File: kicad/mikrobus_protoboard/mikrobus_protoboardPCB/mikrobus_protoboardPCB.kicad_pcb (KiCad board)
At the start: 2 copper layers, 26.8 x 57.5 mm, 0 parts

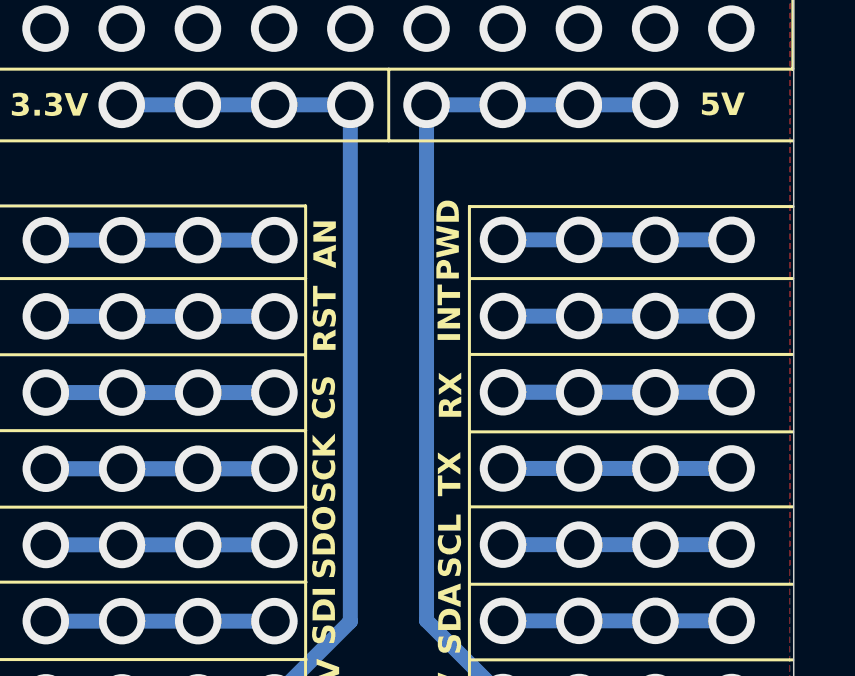
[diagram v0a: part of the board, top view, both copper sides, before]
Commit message: invert RX TX
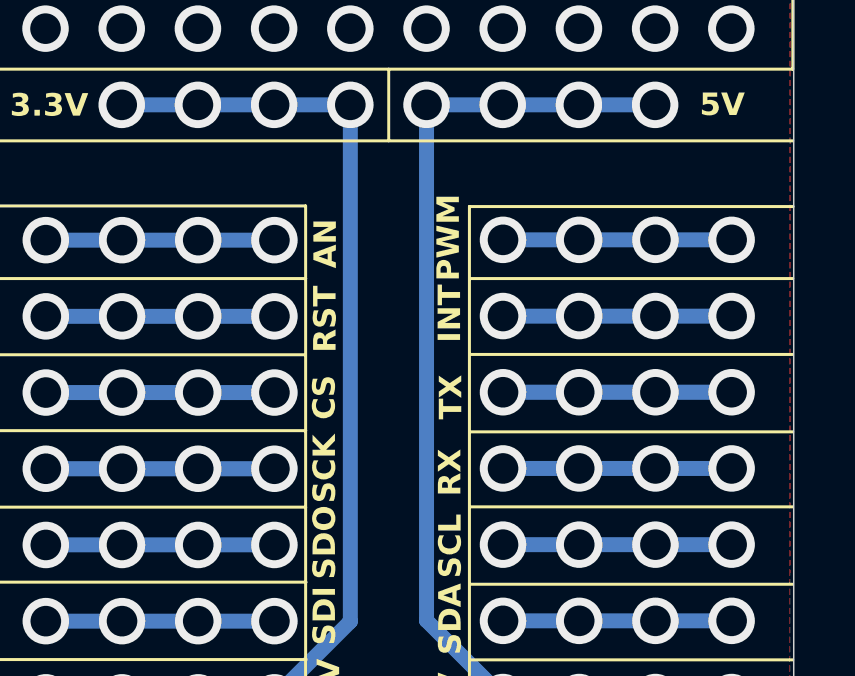
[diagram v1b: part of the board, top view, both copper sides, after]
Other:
- board text added: "PWM"
- board text removed: "PWD"
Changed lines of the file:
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@@
 	)
 	(paper "A4")
+	(title_block
+		(title "Mikrobus Protoboard")
+		(date "2024-09-03")
+		(rev "v1.1")
+		(company "Université Grenoble Alpes - CSUG LIG")
+	)
 	(layers
 		(0 "F.Cu" signal)
@@
 		)
 	)
-	(gr_text "TX"
+	(gr_text "RX"
 		(at 163.66 93.85 90)
 		(layer "F.SilkS")
@@
 		)
 	)
-	(gr_text "PWD"
+	(gr_text "PWM"
 		(at 163.61 86.68 90)
 		(layer "F.SilkS")
@@
 		)
 	)
-	(gr_text "RX"
+	(gr_text "TX"
 		(at 163.69 91.29 90)
 		(layer "F.SilkS")
